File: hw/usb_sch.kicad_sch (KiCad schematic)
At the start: 10 parts, among them J2 USB_C_Receptacle_USB2.0_14P, J3 USB_C_Receptacle_USB2.0_14P

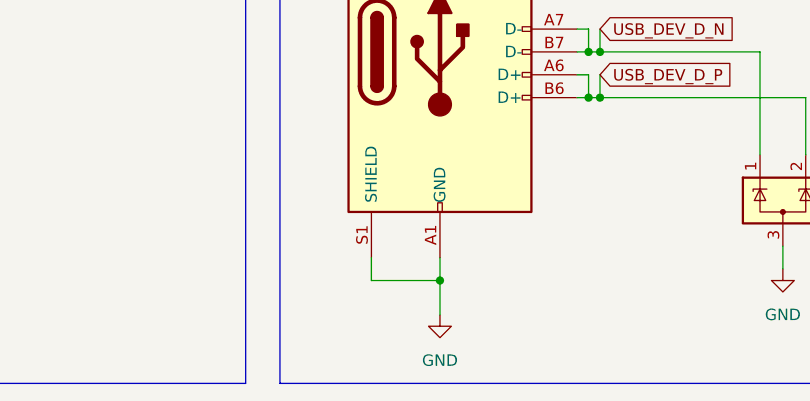
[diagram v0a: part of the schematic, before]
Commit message: changed pcb specs
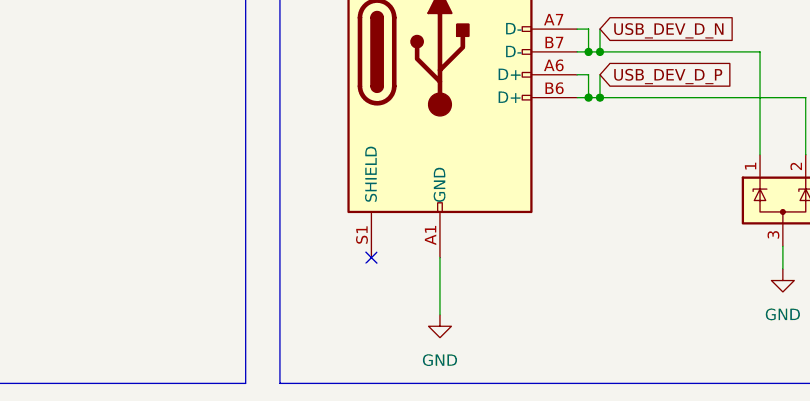
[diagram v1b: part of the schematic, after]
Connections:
- net GND: no longer J2.S1 (SHIELD)
- no-connect marks 1 -> 2
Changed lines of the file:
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@@
-		(color 0 0 0 0)
-	)
-	(junction
-		(at 163.83 78.74)
-		(diameter 0)
 		(color 0 0 0 0)
 	)
@@
 		(at 27.94 76.2)
 	)
+	(no_connect
+		(at 156.21 76.2)
+	)
 	(wire
 		(pts
@@
 	(wire
 		(pts
-			(xy 156.21 76.2) (xy 156.21 78.74)
-		)
-		(stroke
-			(width 0)
-			(type default)
-		)
-	)
-	(wire
-		(pts
 			(xy 52.07 48.26) (xy 52.07 50.8)
 		)
@@
 	(wire
 		(pts
-			(xy 163.83 76.2) (xy 163.83 78.74)
-		)
-		(stroke
-			(width 0)
-			(type default)
-		)
-	)
-	(wire
-		(pts
-			(xy 156.21 78.74) (xy 163.83 78.74)
-		)
-		(stroke
-			(width 0)
-			(type default)
-		)
-	)
-	(wire
-		(pts
 			(xy 77.47 62.23) (xy 77.47 55.88)
 		)
@@
 	(wire
 		(pts
-			(xy 163.83 78.74) (xy 163.83 82.55)
-		)
-		(stroke
+			(xy 163.83 76.2) (xy 163.83 82.55)
+		)
+		(stroke

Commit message: 1p version
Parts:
- removed D2, D3: ESD7L5.0DT5G, Package_TO_SOT_SMD:SOT-723, symbol Power_Protection:ESDA5V3L
- removed D4, D5: 40V 600mV@1A 1A, Diode_SMD:D_SOD-323, symbol Device:D_Schottky
- removed J2, J3: USB_C_Receptacle_USB2.0_14P, Connector_USB:USB_C_Receptacle_GCT_USB4105-xx-A_16P_TopMnt_Horizontal, symbol Connector:USB_C_Receptacle_USB2.0_14P
- removed R2, R3, R4, R5: 5K1, Resistor_SMD:R_0402_1005Metric, symbol Device:R
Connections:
- no-connect marks 2 -> 0
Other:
- note removed: "USB Joystick 2"
